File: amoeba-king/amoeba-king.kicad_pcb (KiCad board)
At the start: 2 copper layers, 19 x 19.1 mm, 12 parts, among them J1 Conn_01x05_Male, J2 Conn_01x05_Male, J3 Conn_01x04_Male, J4 Conn_01x05_Male, J5 Conn_01x01_Male, J6 Conn_01x01_Male

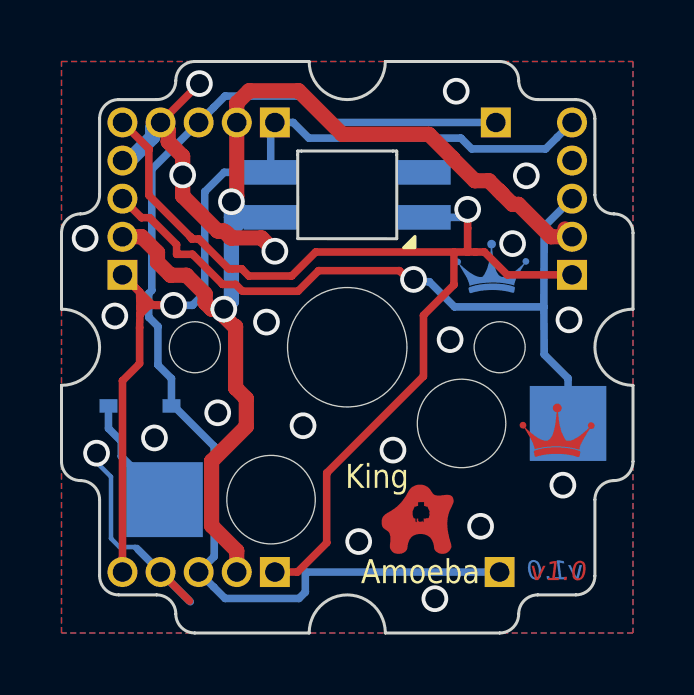
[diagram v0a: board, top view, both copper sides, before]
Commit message: Fixed inverted SMD LED Layout
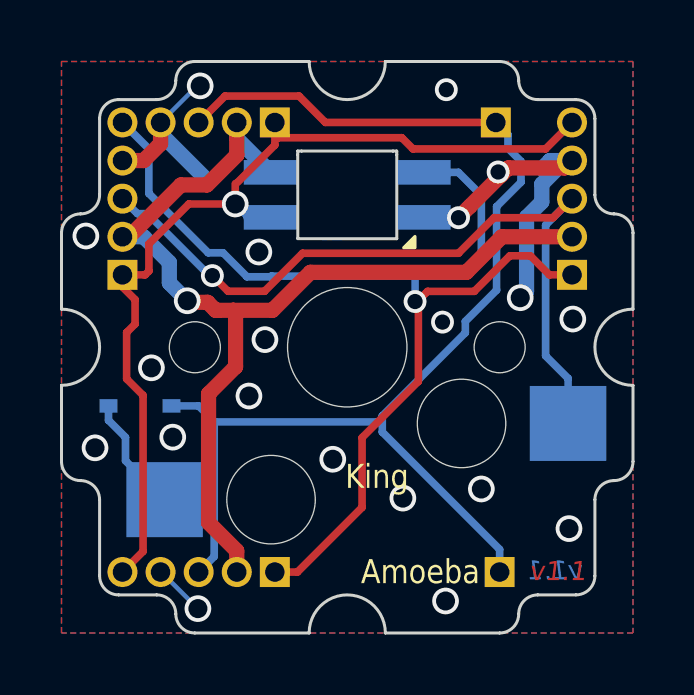
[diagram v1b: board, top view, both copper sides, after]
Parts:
- removed Amoeba-Logo: G***, amoeba-modules:amoeba-logo
- removed Royale (x2): G***, amoeba-modules:royale
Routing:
- net /VDD: track 40.0 -> 35.3 mm, vias 2 -> 1
- net /C: track 38.6 -> 42.0 mm
- net /DIN: track 35.4 -> 38.0 mm
- net /GND: track 18.8 -> 20.7 mm
- net Net-(D1-Pad2): track 5.49 -> 3.90 mm
- net /R: track 24.5 -> 25.7 mm
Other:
- rule via_min_size: 0.889 -> 0.6
- board text added: "v1.1"
- board text removed: "v1.0"

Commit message: Various Layout Improvements
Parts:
- D1: footprint Diode_SMD:D_SOD-323 -> Diode_SMD:D_SOD-123
- moved D1 0.90 mm to (68.4, 169.7), turned to 90 degrees
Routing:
- net /GND: track 20.7 -> 32.1 mm
- net Net-(D1-Pad2): track 3.90 -> 7.08 mm
- net /C: track 42.0 -> 43.0 mm
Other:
- outline, holes or cut-outs redrawn

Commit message: Getting pretty close to v1.1 improved Pads
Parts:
- added Amoeba-Logo-Small: G***, amoeba-modules:amoeba-logo-small, F.Cu at (68.2, 171.3)
- added JP1: SolderJumper_3_Bridged12, amoeba-modules:SolderJumper-3_P1.3mm_Open_RoundedPad1.0x1.5mm, B.Cu at (79.1, 166.8)
- added JP2: SolderJumper_3_Bridged12, amoeba-modules:SolderJumper-3_P1.3mm_Open_RoundedPad1.0x1.5mm, B.Cu at (71.8, 166.8)
- added Royale: G***, amoeba-modules:royale, F.Cu at (69.0, 174.0)
- added Royale: G***, amoeba-modules:royale, B.Cu at (82.1, 174.2)
- J1, J4: value Conn_01x05_Male -> Conn_01x04_Male; footprint amoeba-modules:Header_1x05_P1.27mm -> amoeba-modules:Header_1x04_P1.27mmL
- J2: value Conn_01x05_Male -> Conn_01x04_Male; footprint amoeba-modules:Header_1x05_P1.27mm -> amoeba-modules:Header_1x04_P1.27mm
- moved J1 14.9 mm to (82.9, 165.0), turned to 0 degrees
- moved J4 12.2 mm to (76.8, 176.8), turned to 270 degrees
- moved J2 10.4 mm to (76.8, 160.8), turned to 270 degrees
- moved J5 8.86 mm to (71.7, 176.8), turned to 90 degrees
- moved J6 8.72 mm to (71.7, 160.8), turned to 270 degrees
- moved J3 6.35 mm to (67.9, 165.0), turned to 0 degrees
- moved D1 0.15 mm to (68.3, 169.8), turned to 270 degrees
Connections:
- J1 pad 1: /DIN -> /R
- J1 pad 2: /VDD -> /D1
- J1 pad 3: /C -> /VDD
- J2 pad 1: /DOUT -> /C
- J2 pad 2: /VDD -> /D1
- J2 pad 3: /R -> /VDD
- J3 pad 1: /DOUT -> /R
- J3 pad 2: /VDD -> /D2
- J3 pad 3: /C -> /VDD
- J4 pad 1: /DIN -> /C
- J4 pad 2: /VDD -> /D2
- J4 pad 3: /R -> /VDD
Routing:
- net /DIN: track 38.0 -> 11.2 mm, vias 1 -> 3
- net /GND: track 32.1 -> 12.1 mm, vias 20 -> 21
- net /D2: track 0.00 -> 19.7 mm, vias 0 -> 1
- net /DOUT: track 33.1 -> 14.5 mm, vias 1 -> 0
- net /D1: track 0.00 -> 13.5 mm, vias 0 -> 2
- net /C: track 43.0 -> 31.5 mm
- net /VDD: track 35.3 -> 41.4 mm
- net Net-(D1-Pad2): track 7.08 -> 2.67 mm
- net /R: track 25.7 -> 28.6 mm
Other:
- rule via_min_drill: 0.508 -> 0.3
- board text added: "D1"
- board text added: "D2"

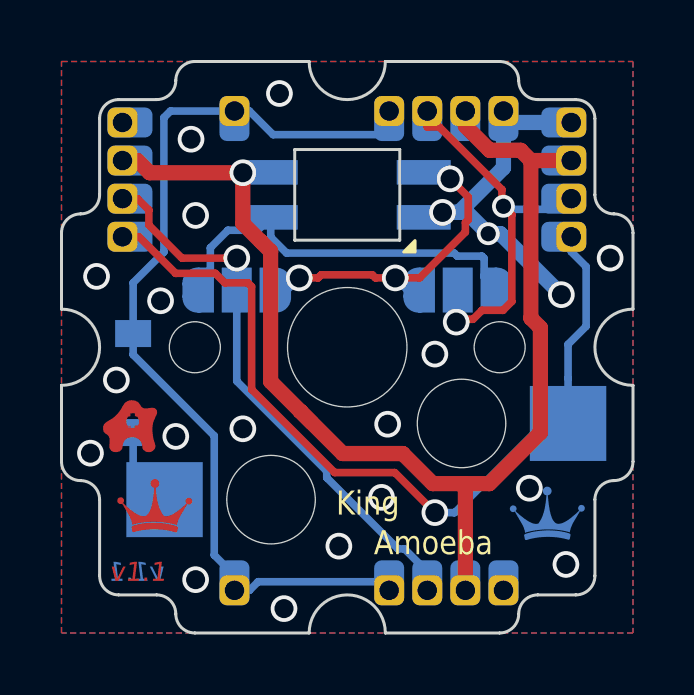
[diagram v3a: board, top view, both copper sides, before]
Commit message: Getting closer to production of 1.1
bigger pads, smaller jumpers
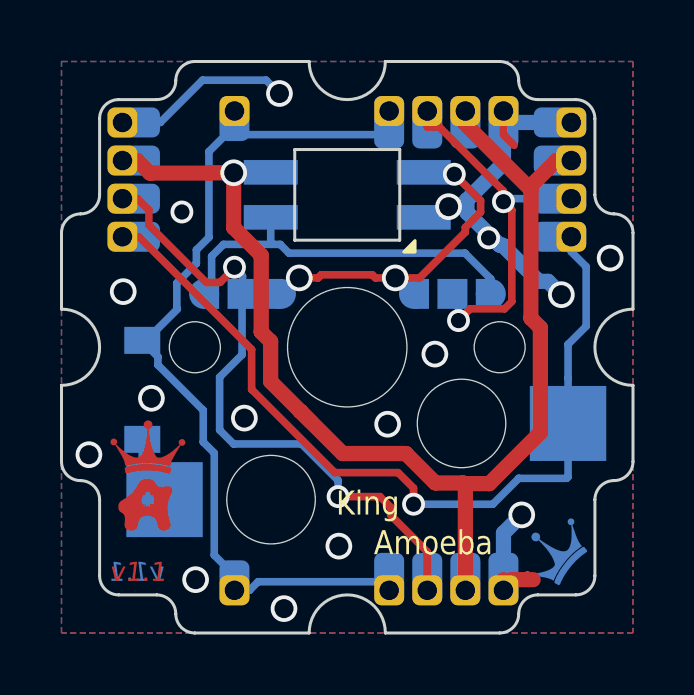
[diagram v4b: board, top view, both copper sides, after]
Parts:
- moved Amoeba-Logo-Small 2.67 mm to (68.8, 173.9)
- moved Royale 1.97 mm to (68.8, 172.0)
- moved Royale 1.26 mm to (82.3, 175.5), turned to 230 degrees
- moved D1 0.38 mm to (68.6, 170.1)
- moved JP2 0.23 mm to (71.9, 166.9)
- moved JP1 0.22 mm to (78.9, 166.9)
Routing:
- net /GND: track 12.1 -> 22.4 mm, vias 21 -> 16
- net /D2: track 19.7 -> 21.7 mm, vias 1 -> 2
- net /DOUT: track 14.5 -> 12.7 mm
- net /C: track 31.5 -> 29.9 mm
- net /VDD: track 41.4 -> 42.4 mm

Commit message: Offset the mounting holes to make more space for cabling
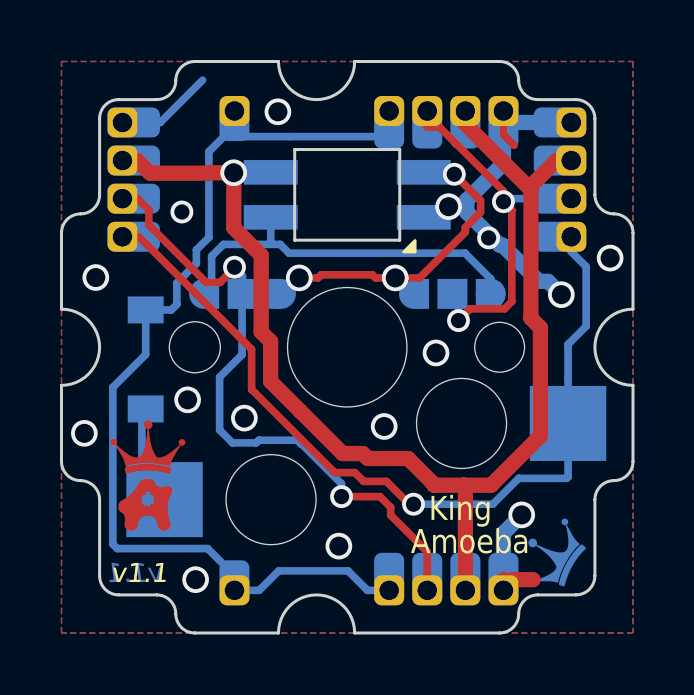
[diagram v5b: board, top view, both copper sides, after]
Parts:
- moved D1 1.02 mm to (68.7, 169.1)
- moved Royale 0.09 mm to (82.3, 175.6), turned to 240 degrees
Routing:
- net /C: track 29.9 -> 33.2 mm
- net /GND: track 22.4 -> 19.7 mm, vias 16 -> 15
- net Net-(D1-Pad2): track 2.32 -> 3.29 mm
- net /VDD: track 42.4 -> 41.8 mm
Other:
- outline, holes or cut-outs redrawn

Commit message: Version 1.2 of the king amoeba.
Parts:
- JP1, JP2: value SolderJumper_3_Bridged12 -> SolderJumper_5; footprint amoeba-modules:SolderJumper-3_P1.3mm_Open_RoundedPad1.0x1.5mm -> amoeba-modules:SolderJumper-5_P1.3mm_Open_RoundedPad1.0x1.5mm
- turned JP1 to 180 degrees
- turned JP2 to 180 degrees
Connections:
- J1 pad 2: /D1 -> Net-(J1-Pad2)
- J2 pad 2: /D1 -> Net-(J2-Pad2)
- J3 pad 2: /D2 -> Net-(J3-Pad2)
- J4 pad 2: /D2 -> Net-(J4-Pad2)
- JP1 pad 1: /DIN -> Net-(J1-Pad2)
- JP1 pad 2: /D1 -> /DIN
- JP1 pad 3: /DOUT -> Net-(J3-Pad2)
- JP2 pad 1: /DOUT -> Net-(J1-Pad2)
- JP2 pad 2: /D2 -> /DOUT
- JP2 pad 3: /DIN -> Net-(J3-Pad2)
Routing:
- net /D2: track 21.7 -> 0.00 mm, vias 2 -> 0
- net Net-(J3-Pad2): track 0.00 -> 21.6 mm, vias 0 -> 3
- net Net-(J4-Pad2): track 0.00 -> 18.6 mm
- net Net-(J1-Pad2): track 0.00 -> 13.9 mm, vias 0 -> 3
- net /D1: track 13.1 -> 0.00 mm, vias 2 -> 0
- net Net-(J2-Pad2): track 0.00 -> 12.5 mm, vias 0 -> 1
- net /DOUT: track 12.7 -> 3.26 mm, vias 0 -> 2
- net /DIN: track 11.4 -> 5.74 mm, vias 3 -> 2
- net /GND: track 19.7 -> 14.5 mm, vias 15 -> 2
- net /C: track 33.2 -> 29.6 mm
- net /R: track 28.2 -> 29.2 mm
- net /VDD: track 41.8 -> 41.3 mm
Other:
- net class Default removed
- board text added: "D"
- board text added: "v1.2"
- board text removed: "D1"
- board text removed: "D2"
- board text removed: "v1.1"
